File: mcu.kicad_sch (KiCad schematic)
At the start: 28 parts, among them SW3 SW_Push, SW4 SW_Push, U2 RP2350_80QFN, Y2 ABM8-272-T3

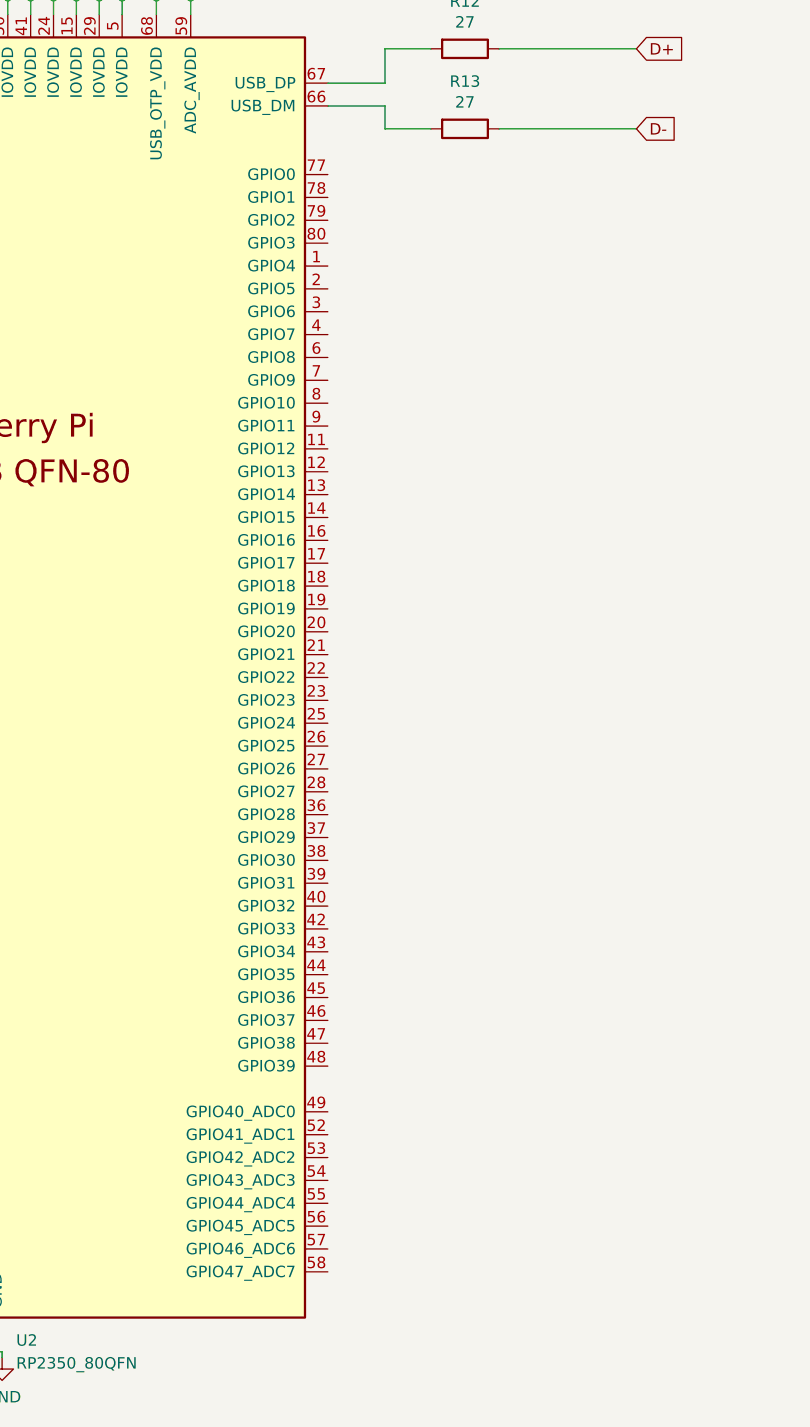
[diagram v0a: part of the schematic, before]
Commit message: add subsheets
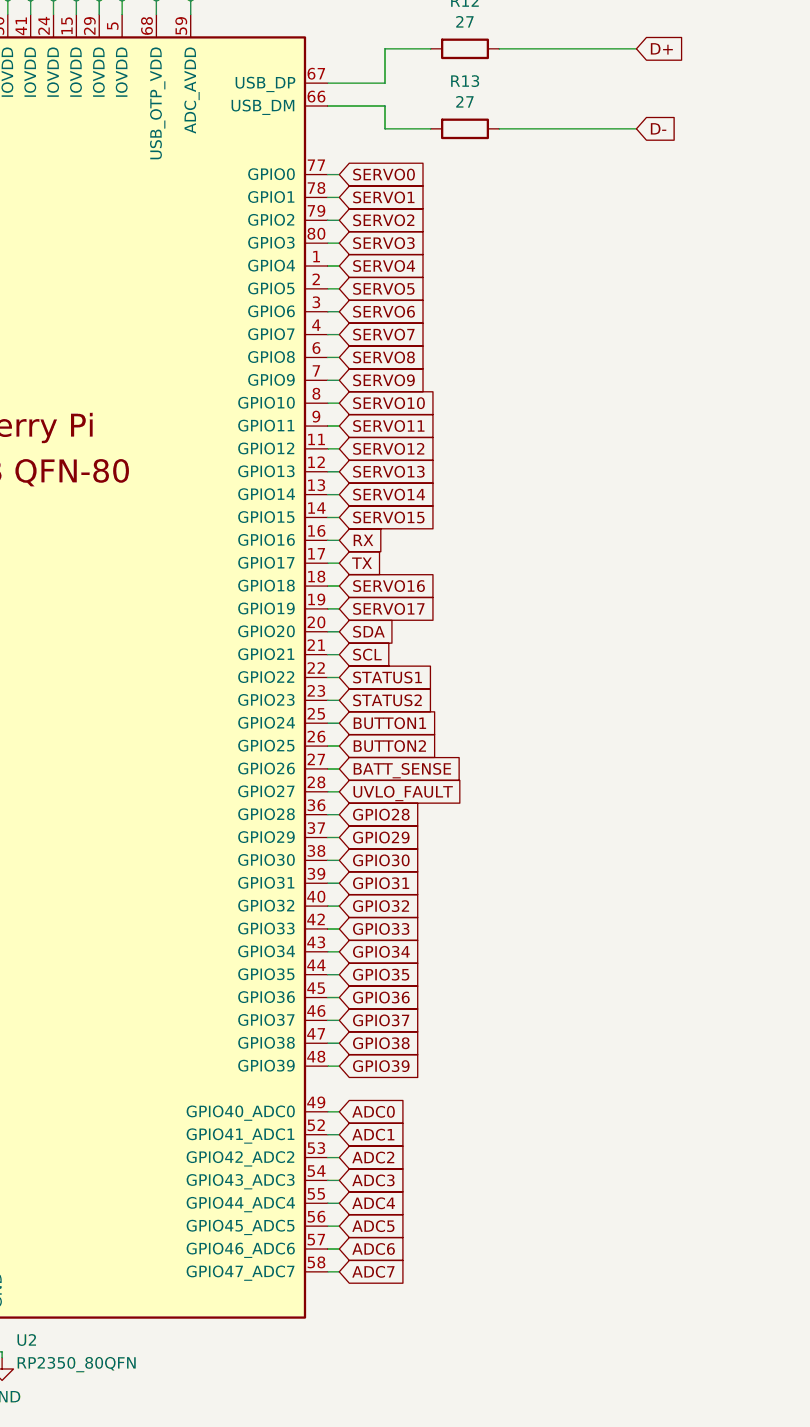
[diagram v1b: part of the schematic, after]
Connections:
- net SERVO4: now reaches U2.1 (GPIO4)
- net SERVO12: now reaches U2.11 (GPIO12)
- net SERVO13: now reaches U2.12 (GPIO13)
- net SERVO14: now reaches U2.13 (GPIO14)
- net SERVO15: now reaches U2.14 (GPIO15)
- net RX: now reaches U2.16 (GPIO16)
- net TX: now reaches U2.17 (GPIO17)
- net SERVO16: now reaches U2.18 (GPIO18)
- net SERVO17: now reaches U2.19 (GPIO19)
- net SERVO5: now reaches U2.2 (GPIO5)
- net SDA: now reaches U2.20 (GPIO20)
- net SCL: now reaches U2.21 (GPIO21)
- net STATUS1: now reaches U2.22 (GPIO22)
- net STATUS2: now reaches U2.23 (GPIO23)
- net BUTTON1: now reaches U2.25 (GPIO24)
- net BUTTON2: now reaches U2.26 (GPIO25)
- net BATT_SENSE: now reaches U2.27 (GPIO26)
- net UVLO_FAULT: now reaches U2.28 (GPIO27)
- net SERVO6: now reaches U2.3 (GPIO6)
- net GPIO28: now reaches U2.36 (GPIO28)
- net GPIO29: now reaches U2.37 (GPIO29)
- net GPIO30: now reaches U2.38 (GPIO30)
- net GPIO31: now reaches U2.39 (GPIO31)
- net SERVO7: now reaches U2.4 (GPIO7)
- net GPIO32: now reaches U2.40 (GPIO32)
- net GPIO33: now reaches U2.42 (GPIO33)
- net GPIO34: now reaches U2.43 (GPIO34)
- net GPIO35: now reaches U2.44 (GPIO35)
- net GPIO36: now reaches U2.45 (GPIO36)
- net GPIO37: now reaches U2.46 (GPIO37)
- net GPIO38: now reaches U2.47 (GPIO38)
- net GPIO39: now reaches U2.48 (GPIO39)
- net ADC0: now reaches U2.49 (GPIO40_ADC0)
- net ADC1: now reaches U2.52 (GPIO41_ADC1)
- net ADC2: now reaches U2.53 (GPIO42_ADC2)
- net ADC3: now reaches U2.54 (GPIO43_ADC3)
- net ADC4: now reaches U2.55 (GPIO44_ADC4)
- net ADC5: now reaches U2.56 (GPIO45_ADC5)
- net ADC6: now reaches U2.57 (GPIO46_ADC6)
- net ADC7: now reaches U2.58 (GPIO47_ADC7)
- net SERVO8: now reaches U2.6 (GPIO8)
- net SERVO9: now reaches U2.7 (GPIO9)
- net SERVO0: now reaches U2.77 (GPIO0)
- net SERVO1: now reaches U2.78 (GPIO1)
- net SERVO2: now reaches U2.79 (GPIO2)
- net SERVO10: now reaches U2.8 (GPIO10)
- net SERVO3: now reaches U2.80 (GPIO3)
- net SERVO11: now reaches U2.9 (GPIO11)
